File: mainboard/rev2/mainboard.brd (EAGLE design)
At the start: 43.2 x 31.8 mm, 82 parts, among them Q1 MOSFET-NCHANNEL2N7002PW, Q2 MOSFET-NCHANNEL2N7002PW, Q3 MOSFET-NCHANNEL2N7002PW, Q4 BSS84, Q5 BSS84, Q6 MOSFET-NCHANNEL2N7002PW, Q7 MOSFET-NCHANNEL2N7002PW, X1 CRYSTAL"32.768"

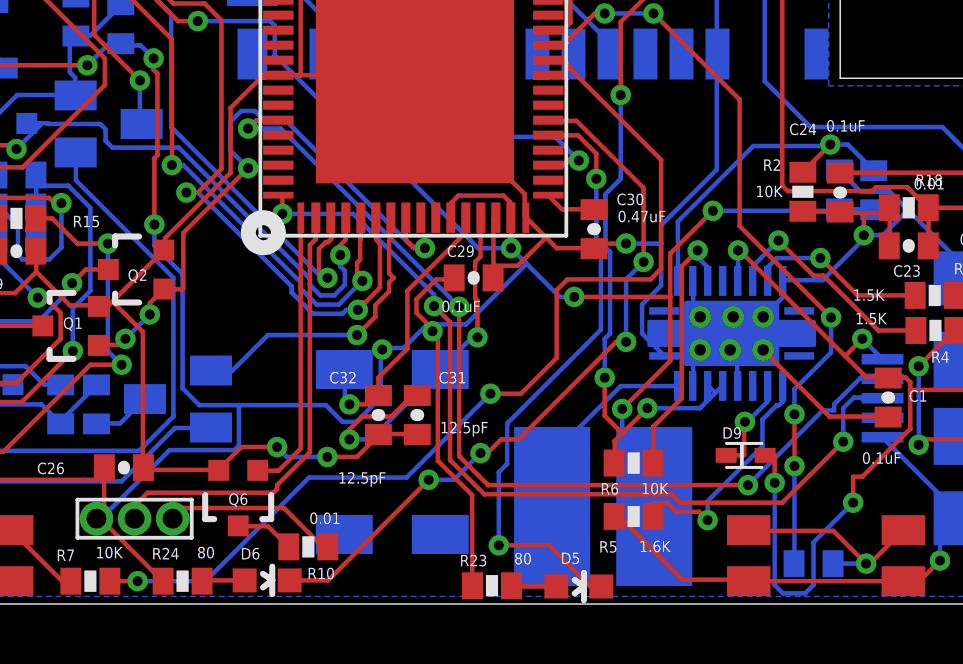
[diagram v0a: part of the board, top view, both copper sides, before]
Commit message: updated rev2 board with part values
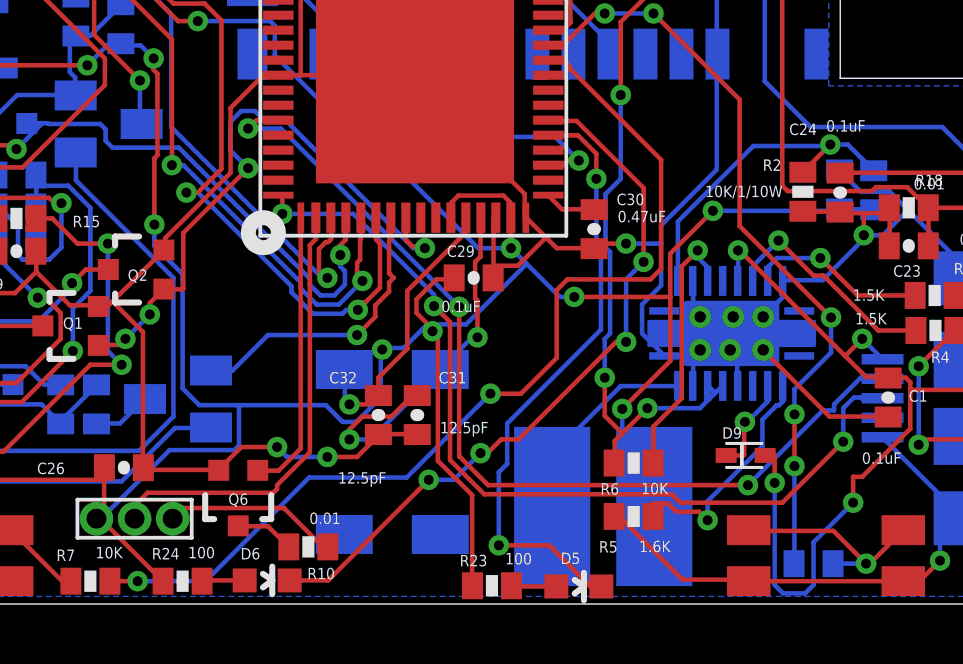
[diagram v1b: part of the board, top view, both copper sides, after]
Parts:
- C10, C11, C12, C13, C17, C18, C4, C5, C7: value (none) -> 2.2u/16v/Y5V
- C14: value (none) -> 100n/16v/X7R
- C15, C16, C6, C8, C9: value (none) -> 2.2u/25v/Y5V
- C19: value (none) -> 2.2u/10v/Y
- C20: value (none) -> 0.1u/16v/Y
- C21: value (none) -> 1u/10v/X7R
- C3: value (none) -> 2.2u/10v/Y5V
- R11: value (none) -> 2k
- R12, R13, R14: value (none) -> 100k
- R15: value (none) -> 0R
- R17: value (none) -> 33k
- R2: value 10K -> 10K/1/10W
- R23, R24: value 80 -> 100
- renumbered U$10 to AP2305
